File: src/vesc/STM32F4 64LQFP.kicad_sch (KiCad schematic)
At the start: 16 parts, among them J5 UNUSED MCU PINS, P5 SWD, U5 STM32F405RGT6, X1 8MHz 10ppm (X50328MSB2GI)

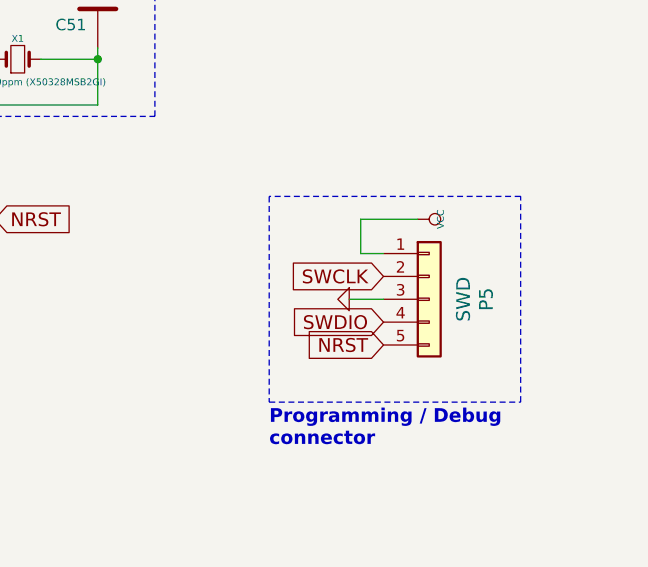
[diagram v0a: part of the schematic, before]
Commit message: remove IMU and servo from schematic
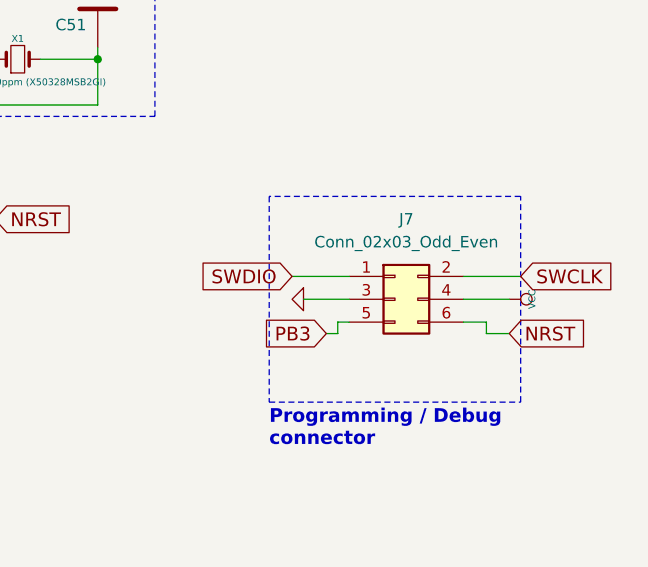
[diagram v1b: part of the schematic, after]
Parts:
- removed P5: SWD, Connector_PinHeader_2.54mm:PinHeader_1x05_P2.54mm_Vertical, symbol Connector_Generic:Conn_01x05
- added J7: Conn_02x03_Odd_Even, symbol Connector_Generic:Conn_02x03_Odd_Even
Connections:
- net GND: now also J7.3 (Pin_3)
- net NRST: now also J7.6 (Pin_6)
- net PB3: now also J7.5 (Pin_5)
- net SWCLK: now also J7.2 (Pin_2)
- net SWDIO: now also J7.1 (Pin_1)
- net VCC: now also J7.4 (Pin_4)
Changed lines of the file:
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@@
 	(wire
 		(pts
+			(xy 242.57 81.28) (xy 242.57 82.55)
+		)
+		(stroke
+			(width 0)
+			(type default)
+		)
+	)
+	(wire
+		(pts
 			(xy 231.14 25.4) (xy 238.76 25.4)
 		)
@@
 	(wire
 		(pts
+			(xy 256.54 78.74) (xy 261.62 78.74)
+		)
+		(stroke
+			(width 0)
+			(type default)
+		)
+	)
+	(wire
+		(pts
 			(xy 181.61 153.67) (xy 181.61 161.29)
 		)
@@
 	(wire
 		(pts
+			(xy 237.49 76.2) (xy 243.84 76.2)
+		)
+		(stroke
+			(width 0)
+			(type default)
+		)
+	)
+	(wire
+		(pts
 			(xy 182.88 125.73) (xy 182.88 128.27)
 		)
@@
 		)
 	)
+	(wire
+		(pts
+			(xy 256.54 76.2) (xy 262.89 76.2)
+		)
+		(stroke
+			(width 0)
+			(type default)
+		)
+	)
 	(polyline
 		(pts
@@
 	(wire
 		(pts
-			(xy 231.14 41.91) (xy 231.14 40.64)
+			(xy 261.62 82.55) (xy 259.08 82.55)
 		)
 		(stroke
@@
 	(wire
 		(pts
-			(xy 187.96 83.82) (xy 185.42 83.82)
+			(xy 231.14 41.91) (xy 231.14 40.64)
 		)
 		(stroke
@@
 	(wire
 		(pts
-			(xy 215.9 39.37) (xy 219.71 39.37)
+			(xy 187.96 83.82) (xy 185.42 83.82)
 		)
 		(stroke
@@
 	(wire
 		(pts
-			(xy 231.14 40.64) (xy 238.76 40.64)
+			(xy 215.9 39.37) (xy 219.71 39.37)
 		)
 		(stroke
@@
 	(wire
 		(pts
-			(xy 245.11 69.85) (xy 245.11 73.66)
+			(xy 231.14 40.64) (xy 238.76 40.64)
 		)
 		(stroke
@@
 	(wire
 		(pts
-			(xy 251.46 69.85) (xy 245.11 69.85)
+			(xy 215.9 52.07) (xy 215.9 57.15)
 		)
 		(stroke
@@
 	(wire
 		(pts
-			(xy 215.9 52.07) (xy 215.9 57.15)
+			(xy 241.3 82.55) (xy 242.57 82.55)
 		)
 		(stroke
@@
 	(wire
 		(pts
+			(xy 259.08 81.28) (xy 259.08 82.55)
+		)
+		(stroke
+			(width 0)
+			(type default)
+		)
+	)
+	(wire
+		(pts
 			(xy 264.16 25.4) (xy 264.16 27.94)
 		)
@@
 	(wire
 		(pts
+			(xy 238.76 78.74) (xy 243.84 78.74)
+		)
+		(stroke
+			(width 0)
+			(type default)
+		)
+	)
+	(wire
+		(pts
 			(xy 203.2 130.81) (xy 203.2 133.35)
 		)
@@
 	(wire
 		(pts
-			(xy 187.96 81.28) (xy 185.42 81.28)
+			(xy 242.57 81.28) (xy 243.84 81.28)
 		)
 		(stroke
@@
 	(wire
 		(pts
-			(xy 247.65 78.74) (xy 243.84 78.74)
+			(xy 187.96 81.28) (xy 185.42 81.28)
 		)
 		(stroke
@@
 	(wire
 		(pts
+			(xy 256.54 81.28) (xy 259.08 81.28)
+		)
+		(stroke
+			(width 0)
+			(type default)
+		)
+	)
+	(wire
+		(pts
 			(xy 257.81 25.4) (xy 257.81 27.94)
 		)
@@
 	(wire
 		(pts
-			(xy 245.11 73.66) (xy 247.65 73.66)
-		)
-		(stroke
-			(width 0)
-			(type default)
-		)
-	)
-	(wire
-		(pts
 			(xy 238.76 25.4) (xy 245.11 25.4)
 		)
@@
 	(global_label "SWDIO"
 		(shape input)
-		(at 247.65 81.28 180)
+		(at 237.49 76.2 180)
 		(effects
 			(font
@@
 		)
 		(property "Intersheetrefs" "${INTERSHEET_REFS}"
-			(at 247.65 81.28 0)
+			(at 237.49 76.2 0)
 			(effects
 				(font
@@
 		)
 	)
+	(global_label "PB3"
+		(shape input)
+		(at 241.3 82.55 180)
+		(effects
+			(font
+				(size 1.524 1.524)
+			)
+			(justify right)
+		)
+		(property "Intersheetrefs" "${INTERSHEET_REFS}"
+			(at 241.3 82.55 0)
+			(effects
+				(font
+					(size 1.27 1.27)
+				)
+				(hide yes)
+			)
+		)
+	)
 	(global_label "PC5"
 		(shape input)
@@
 	(global_label "SWCLK"
 		(shape input)
-		(at 247.65 76.2 180)
+		(at 262.89 76.2 0)
 		(effects
 			(font
 				(size 1.524 1.524)
 			)
-			(justify right)
+			(justify left)
 		)
 		(property "Intersheetrefs" "${INTERSHEET_REFS}"
-			(at 247.65 76.2 0)
+			(at 262.89 76.2 0)
 			(effects
 				(font
@@
 	(global_label "NRST"
 		(shape input)
-		(at 247.65 83.82 180)
+		(at 261.62 82.55 0)
 		(effects
 			(font
 				(size 1.524 1.524)
 			)
-			(justify right)
+			(justify left)
 		)
 		(property "Intersheetrefs" "${INTERSHEET_REFS}"
-			(at 247.65 83.82 0)
+			(at 261.62 82.55 0)
 			(effects
 				(font
@@
 	)
 	(symbol
-		(lib_id "Connector_Generic:Conn_01x05")
-		(at 252.73 78.74 0)
-		(unit 1)
-		(exclude_from_sim no)
-		(in_bom yes)
-		(on_board yes)
-		(dnp no)
-		(property "Reference" "P5"
-			(at 259.08 78.74 90)
-			(effects
-				(font
-					(size 1.524 1.524)
-				)
-			)
-		)
-		(property "Value" "SWD"
-			(at 256.54 78.74 90)
-			(effects
-				(font
-					(size 1.524 1.524)
-				)
-			)
-		)
-		(property "Footprint" "Connector_PinHeader_2.54mm:PinHeader_1x05_P2.54mm_Vertical"
-			(at 252.73 78.74 0)
-			(effects
-				(font
-					(size 1.524 1.524)
-				)
-				(hide yes)
-			)
-		)
-		(property "Datasheet" ""
-			(at 252.73 78.74 0)
-			(effects
-				(font
-					(size 1.524 1.524)
-				)
-				(hide yes)
-			)
-		)
-		(property "Description" ""
-			(at 252.73 78.74 0)
-			(effects
-				(font
-					(size 1.27 1.27)
-				)
-			)
-		)
-		(pin "1"
-		)
-		(pin "2"
-		)
-		(pin "3"
-		)
-		(pin "4"
-		)
-		(pin "5"
-		)
-		(instances
-			(project "Cheap FOCer 2 60mm"
-				(path "/8b53313b-c20e-4d2c-aeda-56c30dbca1c0/00000000-0000-0000-0000-000053f7501a"
-					(reference "P5")
-					(unit 1)
-				)
-			)
-		)
-	)
-	(symbol
 		(lib_id "BLDC_4-rescue:VCC")
-		(at 251.46 69.85 270)
+		(at 261.62 78.74 270)
 		(unit 1)
 		(exclude_from_sim no)
@@
 		(dnp no)
 		(property "Reference" "#PWR074"
-			(at 254 69.85 0)
+			(at 264.16 78.74 0)
 			(effects
 				(font
@@
 		)
 		(property "Value" "VCC"
-			(at 254 69.85 0)
+			(at 264.16 78.74 0)
 			(effects
 				(font
@@
 		)
 		(property "Footprint" ""
-			(at 251.46 69.85 0)
+			(at 261.62 78.74 0)
 			(effects
 				(font
@@
 		)
 		(property "Datasheet" ""
-			(at 251.46 69.85 0)
+			(at 261.62 78.74 0)
 			(effects
 				(font
@@
 		)
 		(property "Description" ""
-			(at 251.46 69.85 0)
+			(at 261.62 78.74 0)
 			(effects
 				(font
@@
 	(symbol
 		(lib_id "BLDC_4-rescue:GND-RESCUE-BLDC_4")
-		(at 243.84 78.74 270)
+		(at 238.76 78.74 270)
 		(unit 1)
 		(exclude_from_sim no)
@@
 		(dnp no)
 		(property "Reference" "#PWR075"
-			(at 243.84 78.74 0)
+			(at 238.76 78.74 0)
 			(effects
 				(font
@@
 		)
 		(property "Value" "GND"
-			(at 242.062 78.74 0)
+			(at 236.982 78.74 0)
 			(effects
 				(font
@@
 		)
 		(property "Footprint" ""
-			(at 243.84 78.74 0)
+			(at 238.76 78.74 0)
 			(effects
 				(font
@@
 		)
 		(property "Datasheet" ""
-			(at 243.84 78.74 0)
+			(at 238.76 78.74 0)
 			(effects
 				(font
@@
 		)
 		(property "Description" ""
-			(at 243.84 78.74 0)
+			(at 238.76 78.74 0)
 			(effects
 				(font
@@
 					(unit 1)
 				)
+			)
+		)
+	)
+	(symbol
+		(lib_id "Connector_Generic:Conn_02x03_Odd_Even")
+		(at 248.92 78.74 0)
+		(unit 1)
+		(exclude_from_sim no)
+		(in_bom yes)
+		(on_board yes)
+		(dnp no)
+		(fields_autoplaced yes)
+		(property "Reference" "J7"
+			(at 250.19 69.85 0)
+			(effects
+				(font
+					(size 1.27 1.27)
+				)
+			)
+		)
+		(property "Value" "Conn_02x03_Odd_Even"
+			(at 250.19 72.39 0)
+			(effects
+				(font
+					(size 1.27 1.27)
+				)
+			)
+		)
+		(property "Footprint" ""
+			(at 248.92 78.74 0)
+			(effects
+				(font
+					(size 1.27 1.27)
+				)
+				(hide yes)
+			)
+		)
+		(property "Datasheet" "~"
+			(at 248.92 78.74 0)
+			(effects
+				(font
+					(size 1.27 1.27)
+				)
+				(hide yes)
+			)
+		)
+		(property "Description" "Generic connector, double row, 02x03, odd/even pin numbering scheme (row 1 odd numbers, row 2 even numbers), script generated (kicad-library-utils/schlib/autogen/connector/)"
+			(at 248.92 78.74 0)
+			(effects
+				(font
+					(size 1.27 1.27)
+				)
+				(hide yes)
+			)
+		)
+		(pin "3"
+		)
+		(pin "1"
+		)
+		(pin "4"
+		)
+		(pin "5"
+		)
+		(pin "2"
+		)
+		(pin "6"
+		)
+		(instances
+			(project ""
+				(path "/8b53313b-c20e-4d2c-aeda-56c30dbca1c0/00000000-0000-0000-0000-000053f7501a"
+					(reference "J7")
+					(unit 1)
+				)

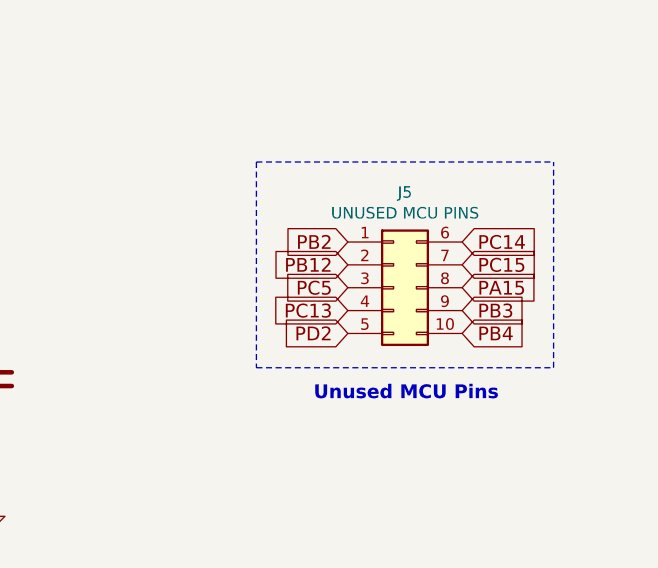
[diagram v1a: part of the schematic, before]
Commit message: Removed unused 10 pin MCU header
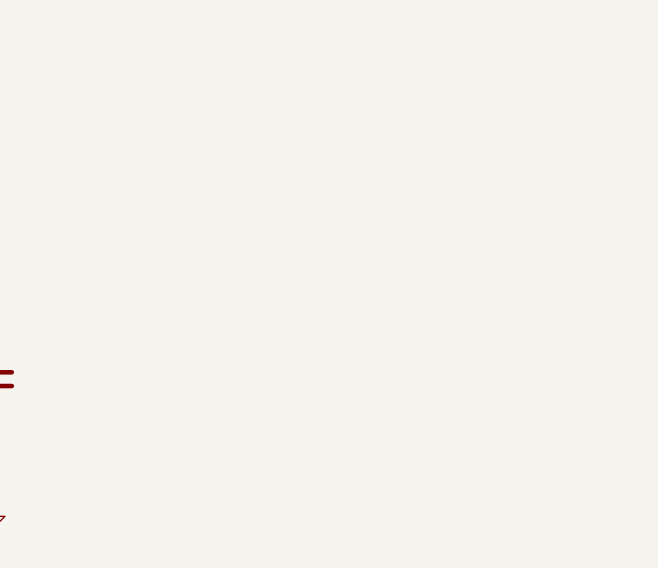
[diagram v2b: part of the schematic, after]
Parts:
- removed J5: UNUSED MCU PINS, Connector_PinHeader_2.00mm:PinHeader_2x05_P2.00mm_Vertical, symbol Connector_Generic:Conn_02x05_Top_Bottom
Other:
- note removed: "Unused MCU Pins"

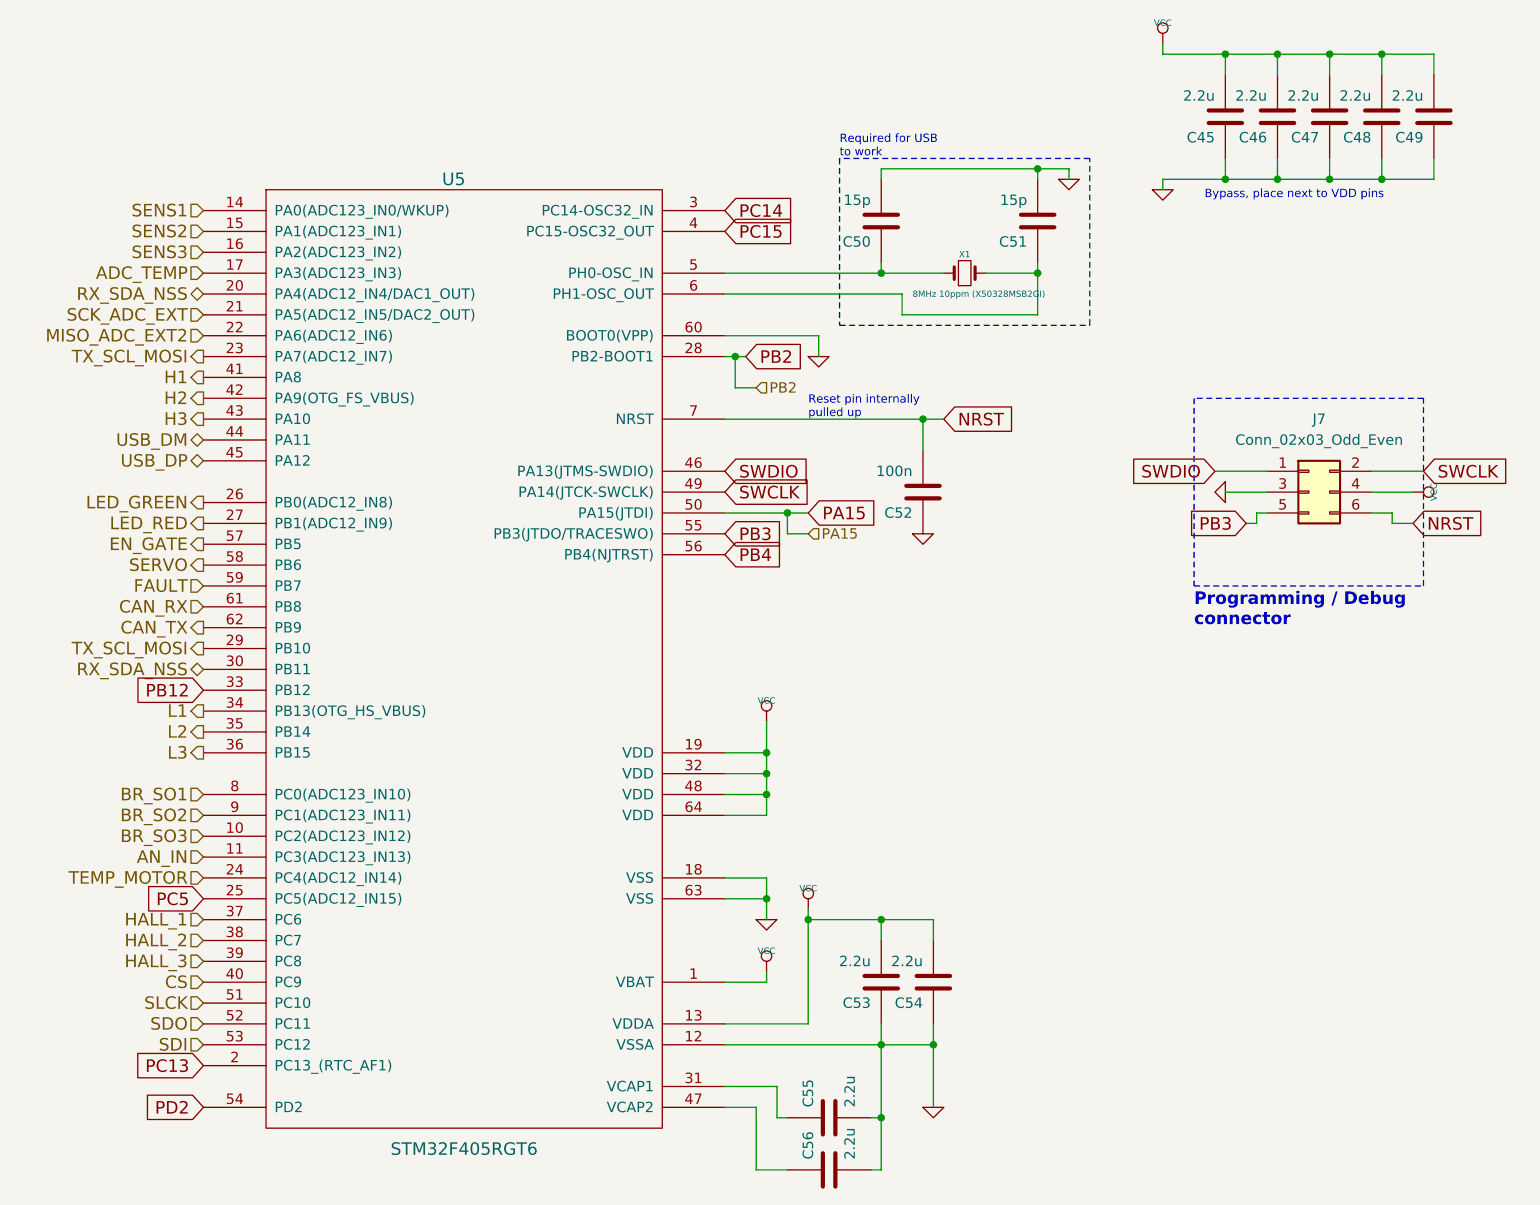
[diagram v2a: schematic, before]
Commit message: Fix component values
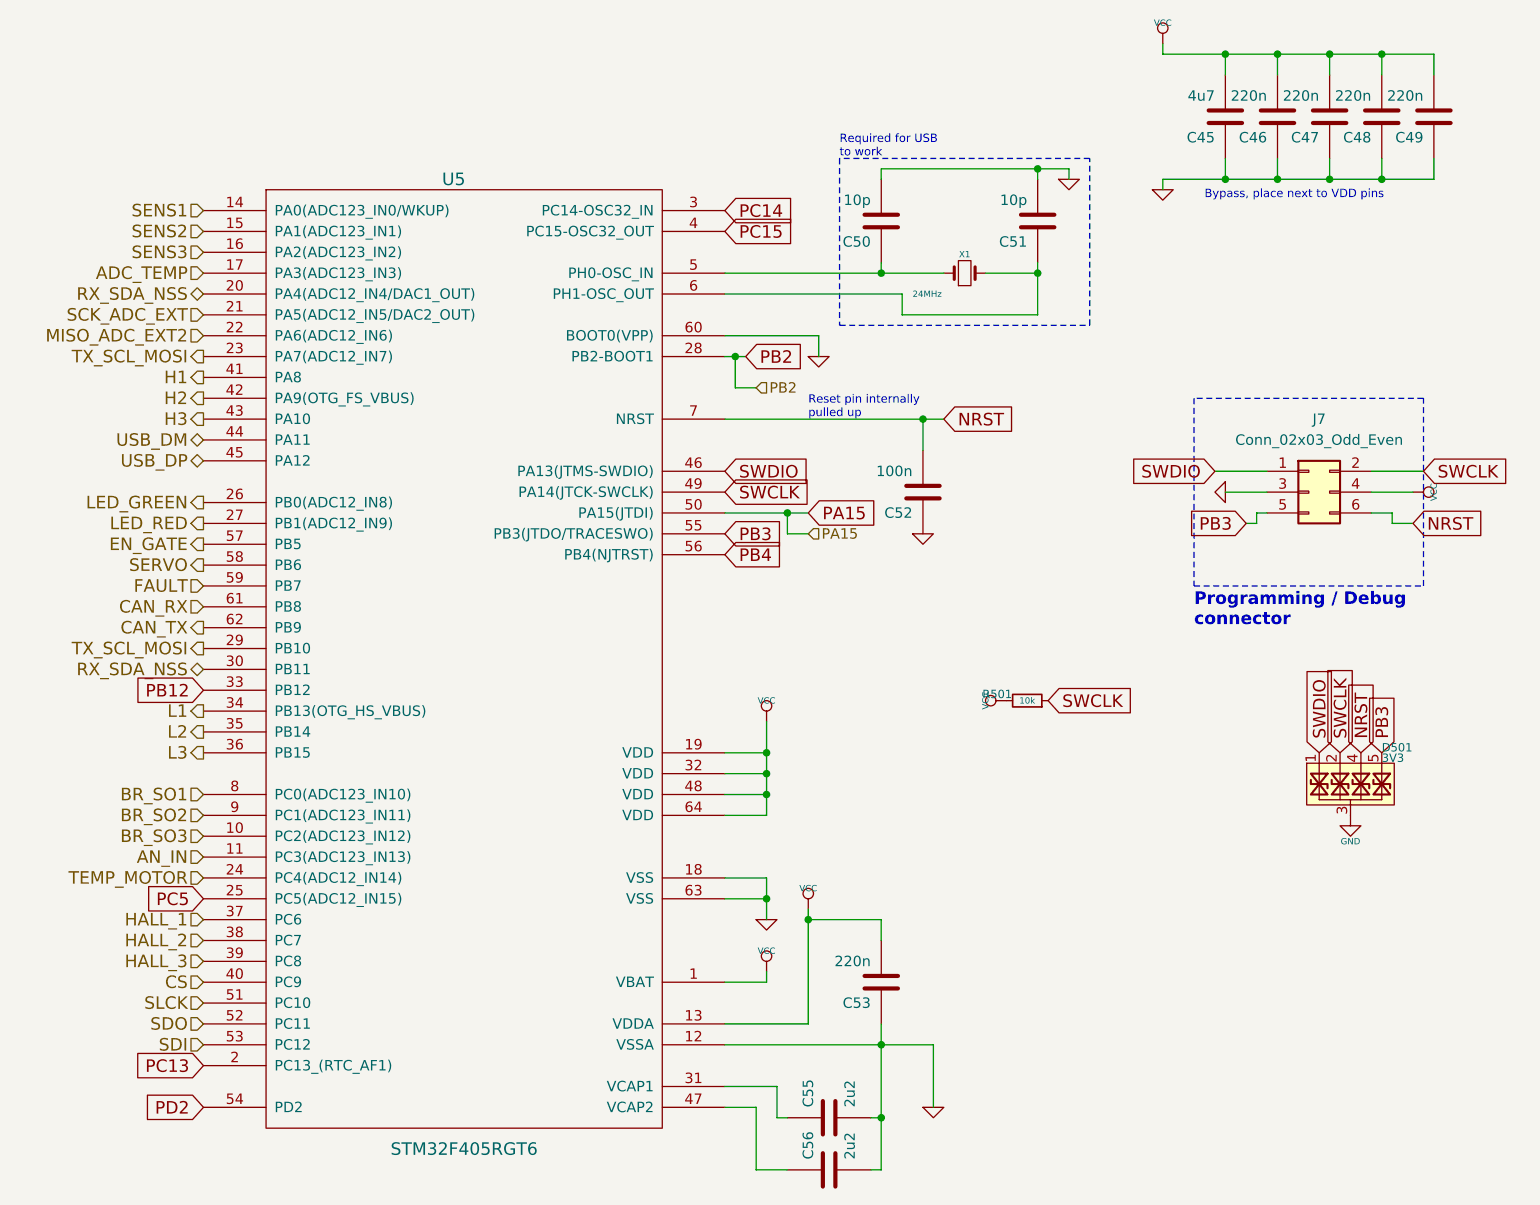
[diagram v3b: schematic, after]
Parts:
- removed C54: 2.2u, Capacitor_SMD:C_0603_1608Metric, symbol BLDC_4-rescue:C-RESCUE-BLDC_4
- added D501: 3V3, symbol Bluesat:D_TVS_Quad_Compact
- added R501: 10k, symbol Bluesat:R_CompactH
- C45: value 2.2u -> 4u7; footprint Capacitor_SMD:C_0603_1608Metric -> (none)
- C46, C47, C48, C49, C53: value 2.2u -> 220n; footprint Capacitor_SMD:C_0603_1608Metric -> (none)
- C50, C51: value 15p -> 10p; footprint Capacitor_SMD:C_0603_1608Metric -> (none)
- C52: footprint Capacitor_SMD:C_0603_1608Metric -> (none)
- C55, C56: value 2.2u -> 2u2; footprint Capacitor_SMD:C_0603_1608Metric -> (none)
- U5: footprint Package_QFP:LQFP-64_10x10mm_P0.5mm -> (none)
- X1: value 8MHz 10ppm (X50328MSB2GI) -> 24MHz; footprint Crystal:Crystal_SMD_5032-2Pin_5.0x3.2mm -> (none)
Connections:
- net GND: now also D501.3, D501.8
- net NRST: now also D501.4, D501.7
- net PB3: now also D501.5, D501.6
- net SWCLK: now also D501.2, D501.9, R501.1
- net SWDIO: now also D501.1, D501.10
- net VCC: now also R501.2

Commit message: footprints - most resistors and caps, some ICs
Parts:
- C45: footprint (none) -> Capacitor_SMD:C_0805_2012Metric
- C46, C47, C48, C49, C50, C51, C52, C53: footprint (none) -> Capacitor_SMD:C_0402_1005Metric
- C55, C56: footprint (none) -> Capacitor_SMD:C_0201_0603Metric
- D501: footprint (none) -> Package_DFN_QFN:Diodes_UDFN-10_1.0x2.5mm_P0.5mm
- R501: footprint (none) -> Resistor_SMD:R_0402_1005Metric
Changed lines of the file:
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@@
 			)
 		)
-		(property "Footprint" ""
+		(property "Footprint" "Capacitor_SMD:C_0201_0603Metric"
 			(at 190.5 161.29 0)
 			(effects
@@
 			)
 		)
-		(property "Footprint" ""
+		(property "Footprint" "Capacitor_SMD:C_0201_0603Metric"
 			(at 190.5 154.94 0)
 			(effects
@@
 			)
 		)
-		(property "Footprint" ""
+		(property "Footprint" "Capacitor_SMD:C_0402_1005Metric"
 			(at 196.85 45.72 0)
 			(effects
@@
 			)
 		)
-		(property "Footprint" ""
+		(property "Footprint" "Capacitor_SMD:C_0402_1005Metric"
 			(at 215.9 45.72 0)
 			(effects
@@
 			)
 		)
-		(property "Footprint" ""
+		(property "Footprint" "Capacitor_SMD:C_0402_1005Metric"
 			(at 196.85 138.43 0)
 			(effects
@@
 			)
 		)
-		(property "Footprint" ""
+		(property "Footprint" "Capacitor_SMD:C_0402_1005Metric"
 			(at 201.93 78.74 0)
 			(effects
@@
 			)
 		)
-		(property "Footprint" ""
+		(property "Footprint" "Capacitor_SMD:C_0805_2012Metric"
 			(at 238.76 33.02 0)
 			(effects
@@
 			)
 		)
-		(property "Footprint" ""
+		(property "Footprint" "Capacitor_SMD:C_0402_1005Metric"
 			(at 245.11 33.02 0)
 			(effects
@@
 			)
 		)
-		(property "Footprint" ""
+		(property "Footprint" "Capacitor_SMD:C_0402_1005Metric"
 			(at 264.16 33.02 0)
 			(effects
@@
 			)
 		)
-		(property "Footprint" ""
+		(property "Footprint" "Capacitor_SMD:C_0402_1005Metric"
 			(at 251.46 33.02 0)
 			(effects
@@
 			)
 		)
-		(property "Footprint" ""
+		(property "Footprint" "Capacitor_SMD:C_0402_1005Metric"
 			(at 257.81 33.02 0)
 			(effects
@@
 			)
 		)
-		(property "Footprint" ""
+		(property "Footprint" "Resistor_SMD:R_0402_1005Metric"
 			(at 214.63 104.14 90)
 			(effects
@@
 			)
 		)
-		(property "Footprint" ""
+		(property "Footprint" "Package_DFN_QFN:Diodes_UDFN-10_1.0x2.5mm_P0.5mm"
 			(at 254 114.3 0)
 			(effects

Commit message: footprints for remaining caps, resistors, diodes, MOSFETs. and ICs
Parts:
- C55, C56: footprint Capacitor_SMD:C_0201_0603Metric -> Capacitor_SMD:C_0603_1608Metric
- U5: footprint (none) -> CRF1:lqfp64_pad_mod
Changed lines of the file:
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@@
 			)
 		)
-		(property "Footprint" ""
+		(property "Footprint" "CRF1:lqfp64_pad_mod"
 			(at 146.05 99.06 0)
 			(effects
@@
 			)
 		)
-		(property "Footprint" "Capacitor_SMD:C_0201_0603Metric"
+		(property "Footprint" "Capacitor_SMD:C_0603_1608Metric"
 			(at 190.5 161.29 0)
 			(effects
@@
 			)
 		)
-		(property "Footprint" "Capacitor_SMD:C_0201_0603Metric"
+		(property "Footprint" "Capacitor_SMD:C_0603_1608Metric"
 			(at 190.5 154.94 0)
 			(effects
